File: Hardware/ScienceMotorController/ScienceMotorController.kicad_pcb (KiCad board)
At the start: 2 copper layers, 124.5 x 116.6 mm, 122 parts, among them U1 LM2576D2TR4, U2 TM4C129E_Launchpad, U3 VNH5019A_E, U4 VNH5019A_E, U5 VNH5019A_E, U6 VNH5019A_E, U7 VNH5019A_E, U8 VNH5019A_E

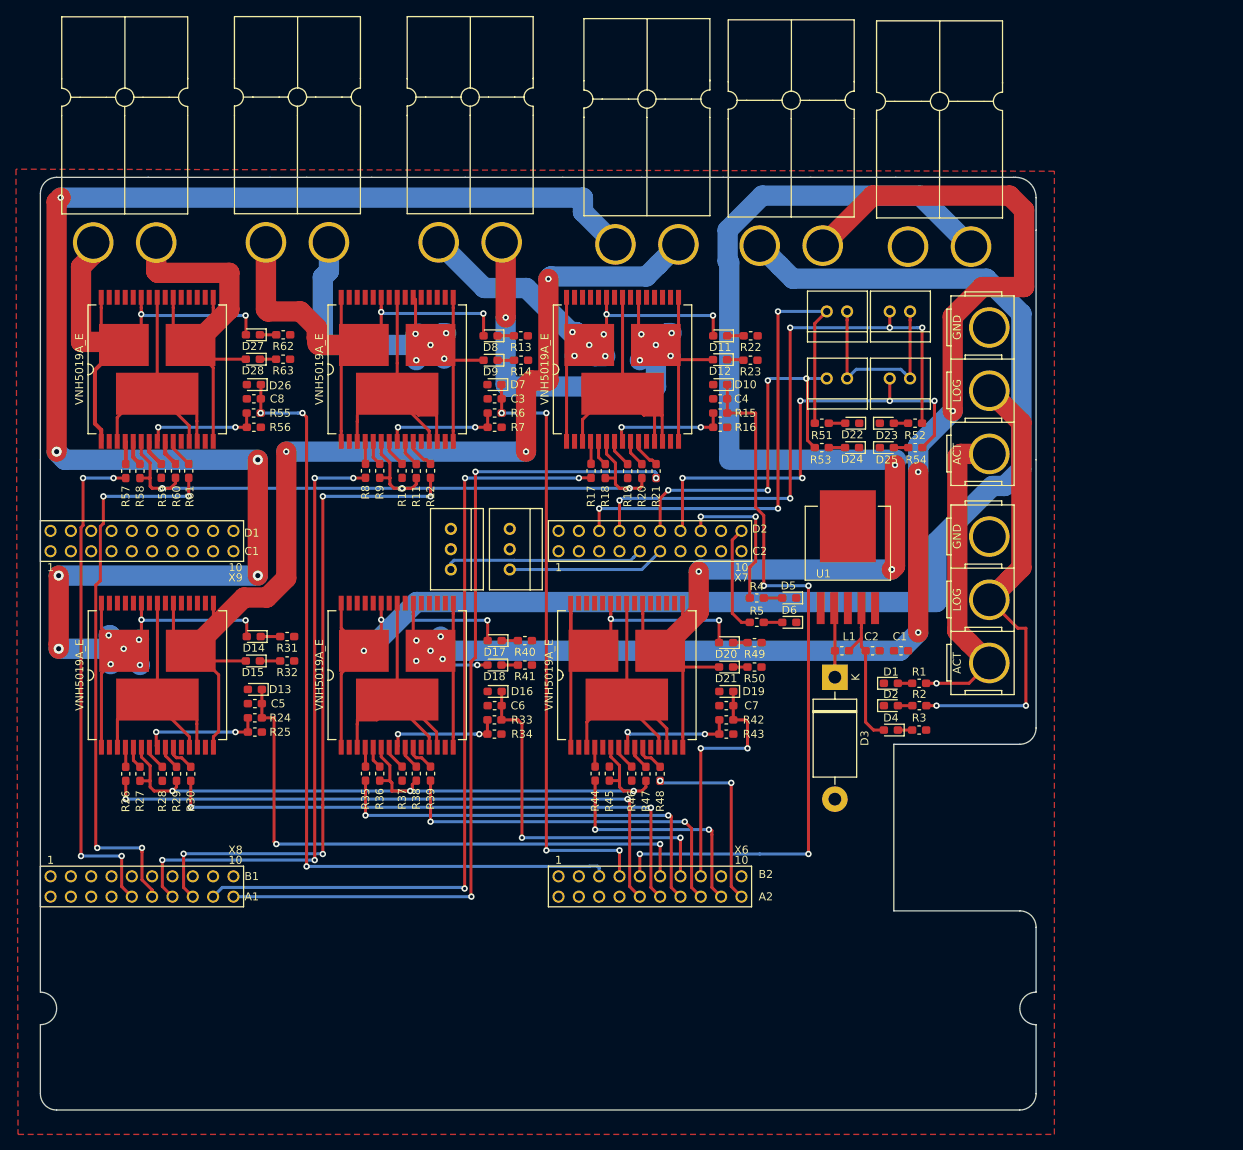
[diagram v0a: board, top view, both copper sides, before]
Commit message: routed more traces
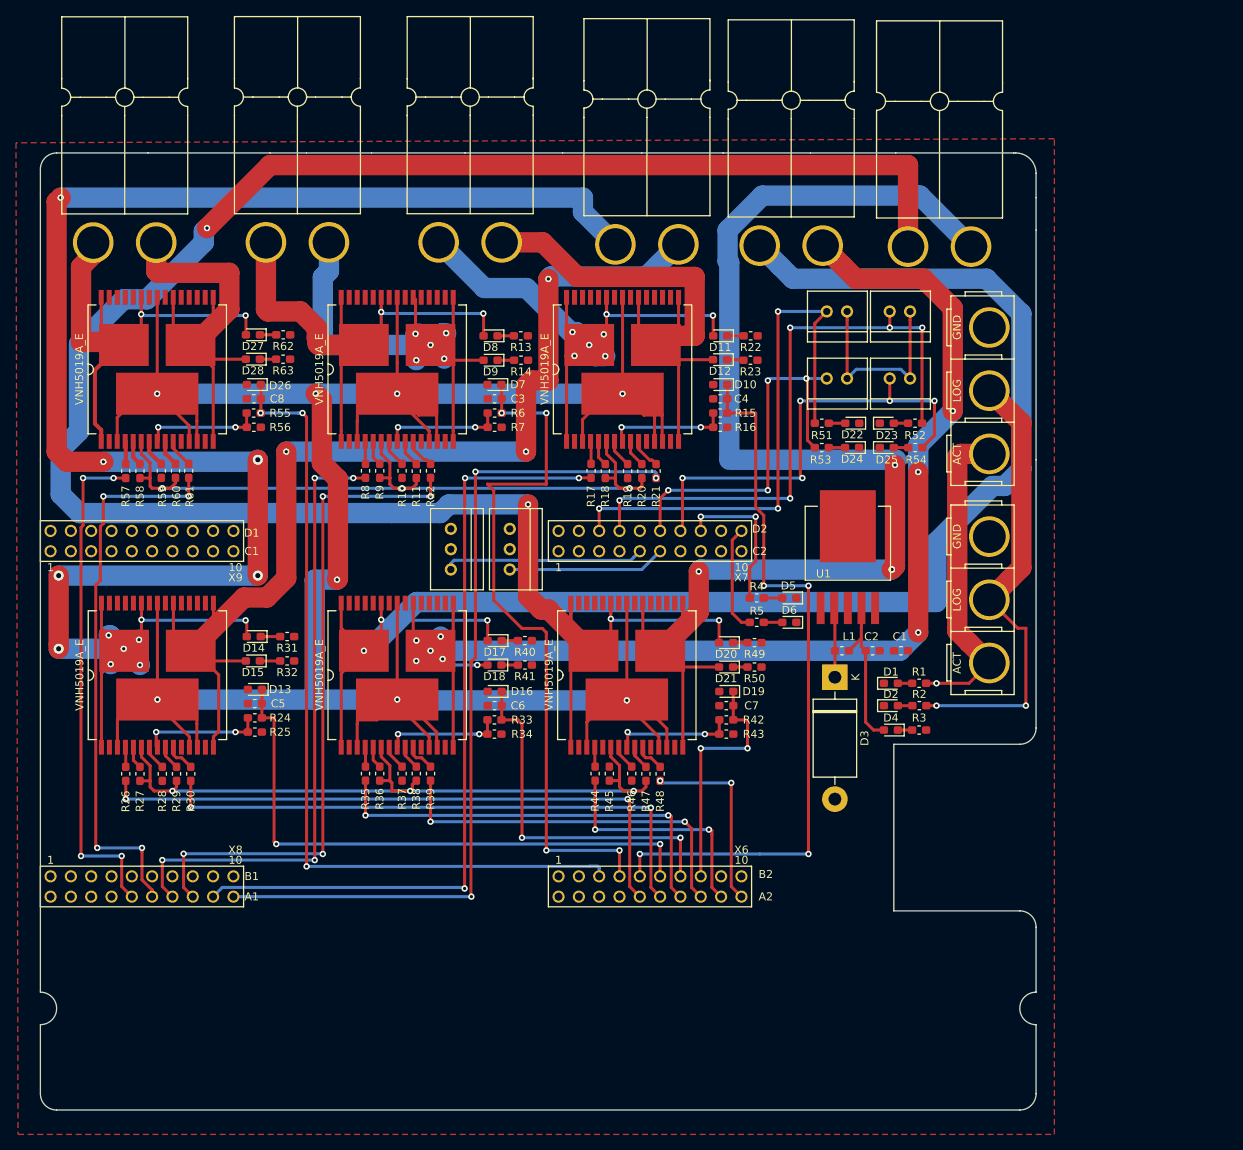
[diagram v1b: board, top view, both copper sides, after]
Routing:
- net Net-(Conn7-Pad2): track 49.0 -> 274.4 mm, vias 2 -> 4
- net +12VA: track 246.9 -> 406.0 mm, vias 1 -> 9
- net Net-(Conn6-Pad1): track 197.6 -> 169.9 mm
- net Net-(Conn4-Pad1): track 85.3 -> 70.3 mm, vias 6 -> 0
- net /Tiva/Motor Driver 2/Current_Sense_2: track 76.3 -> 88.2 mm
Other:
- board size 124.5 x 116.6 mm -> 124.5 x 119.6 mm

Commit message: finished routing traces
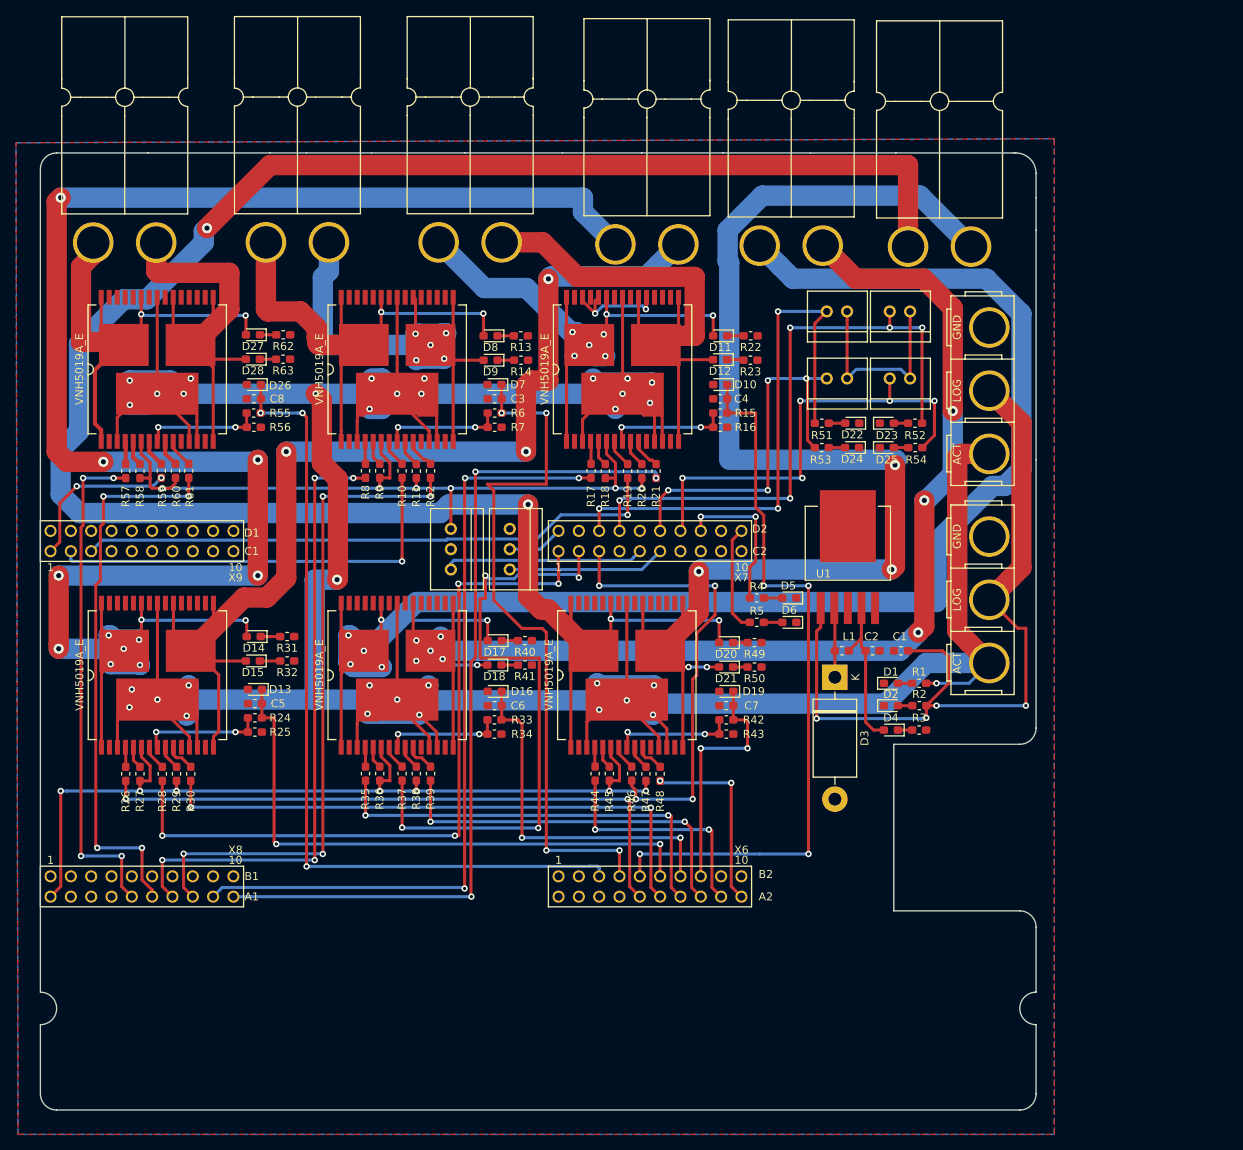
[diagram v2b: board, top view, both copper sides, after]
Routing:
- net +12VA: track 406.0 -> 551.6 mm, vias 9 -> 34
- net /Tiva/Motor Driver 4/PWM_4: track 0.00 -> 92.5 mm, vias 0 -> 4
- net /Tiva/Motor Driver 5/PWM_5: track 0.00 -> 78.0 mm, vias 0 -> 4
- net /Tiva/Motor Driver 3/PWM_3: track 0.00 -> 73.5 mm, vias 0 -> 1
- net /Tiva/Motor Driver 6/PWM_6: track 0.00 -> 56.3 mm, vias 0 -> 4
- net /Tiva/Motor Driver 2/PWM_2: track 0.00 -> 53.0 mm, vias 0 -> 1
- net /Power/12V: track 57.6 -> 99.6 mm, vias 2 -> 4
- net /Power/3.3V: track 229.8 -> 252.0 mm, vias 6 -> 13
- net /Tiva/Motor Driver 1/PWM_1: track 0.00 -> 20.5 mm, vias 0 -> 2
- net GND: track 0.00 -> 20.3 mm, vias 0 -> 2
- net Net-(Conn6-Pad2): track 194.7 -> 208.7 mm, vias 3 -> 6
- net Net-(Conn5-Pad2): track 241.0 -> 248.7 mm
- net Net-(Conn3-Pad1): track 68.5 -> 75.9 mm
- net Net-(R45-Pad1): track 0.00 -> 2.76 mm
- net Net-(Conn7-Pad1): vias 4 -> 5
- added copper zone on B.Cu, net /Power/3.3V

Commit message: fixed islands
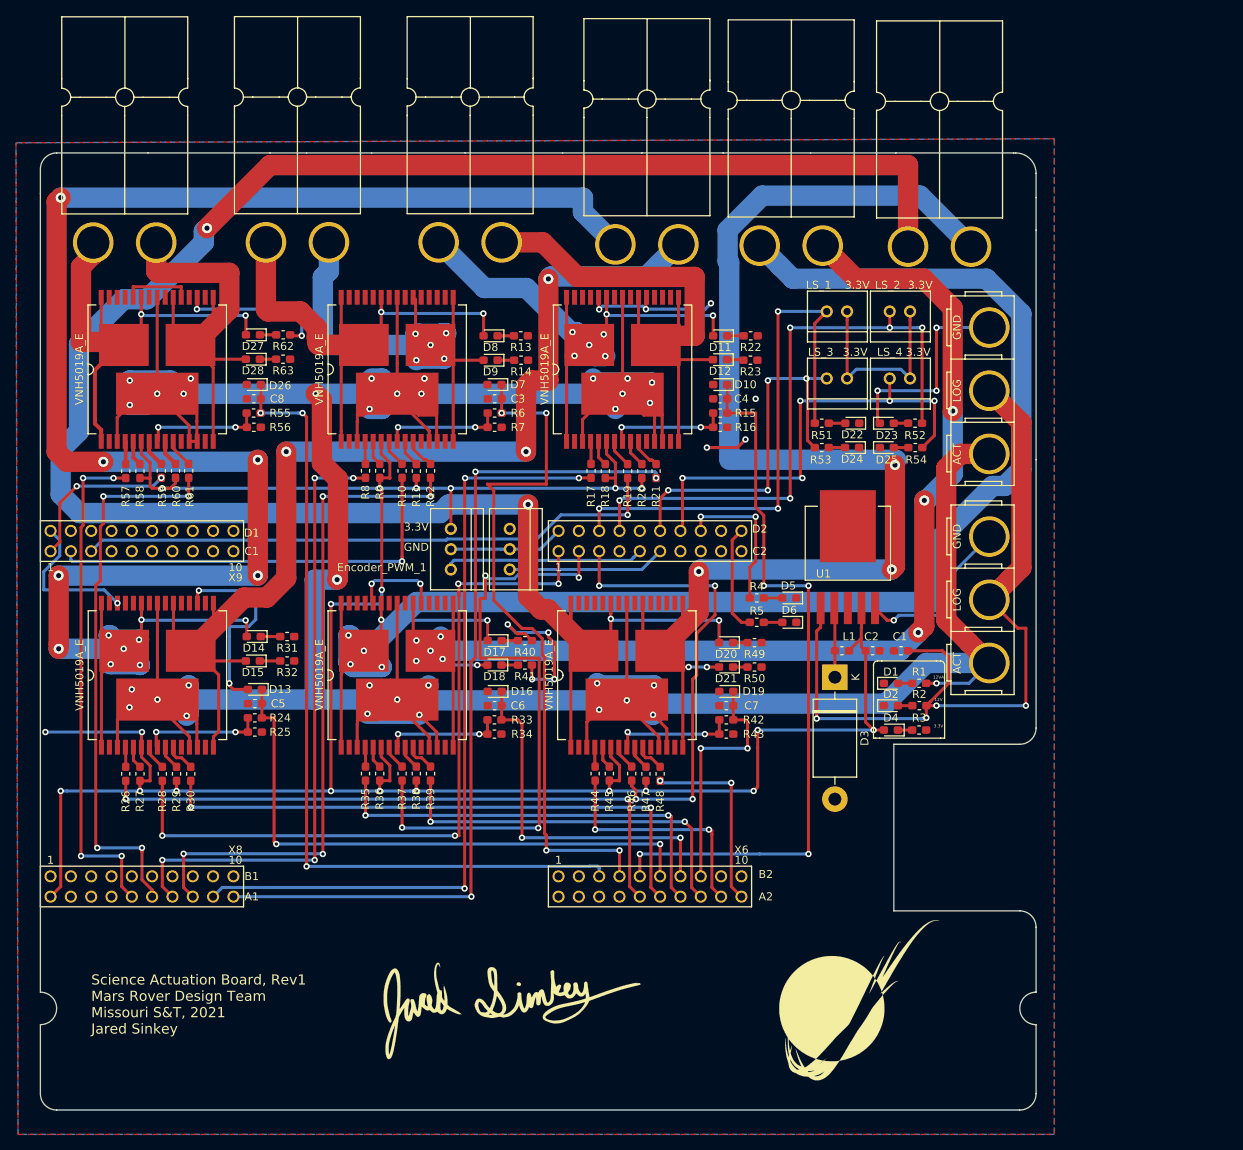
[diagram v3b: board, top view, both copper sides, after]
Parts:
- added G***: LOGO, MRDT_Silkscreens:0_MRDT_Logo_20mm, F.Cu at (136.9, 145.3)
- added G***: LOGO, MRDT_Silkscreens:0_MRDT_Logo_50mm, B.Cu at (110.2, 79.2)
- added G***: LOGO, MRDT_Silkscreens:z_sig_Jared_Sinkey_15.5mmx34.4mm, F.Cu at (93.7, 146.1)
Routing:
- net GND: track 20.3 -> 183.0 mm, vias 2 -> 18
- net /Power/3.3V: track 252.0 -> 351.3 mm, vias 13 -> 24
- net +12VA: track 551.6 -> 554.4 mm
- net Net-(Conn5-Pad1): track 139.0 -> 140.4 mm
- net /Tiva/Motor Driver 2/Current_Sense_2: track 88.2 -> 87.4 mm
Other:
- board text added: "12V"
- board text added: "12VA"
- board text added: "3.3V"
- board text added: "Encoder_PWM_1"
- board text added: "GND"
- board text added: "LS_1"
- board text added: "LS_2"
- board text added: "LS_3"
- board text added: "LS_4"
- board text added: "Science Actuation Board, Rev1 Mars Rover Design Team Missouri S&T, 2021 Jared Sinkey"

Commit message: added oki and began rerouting traces
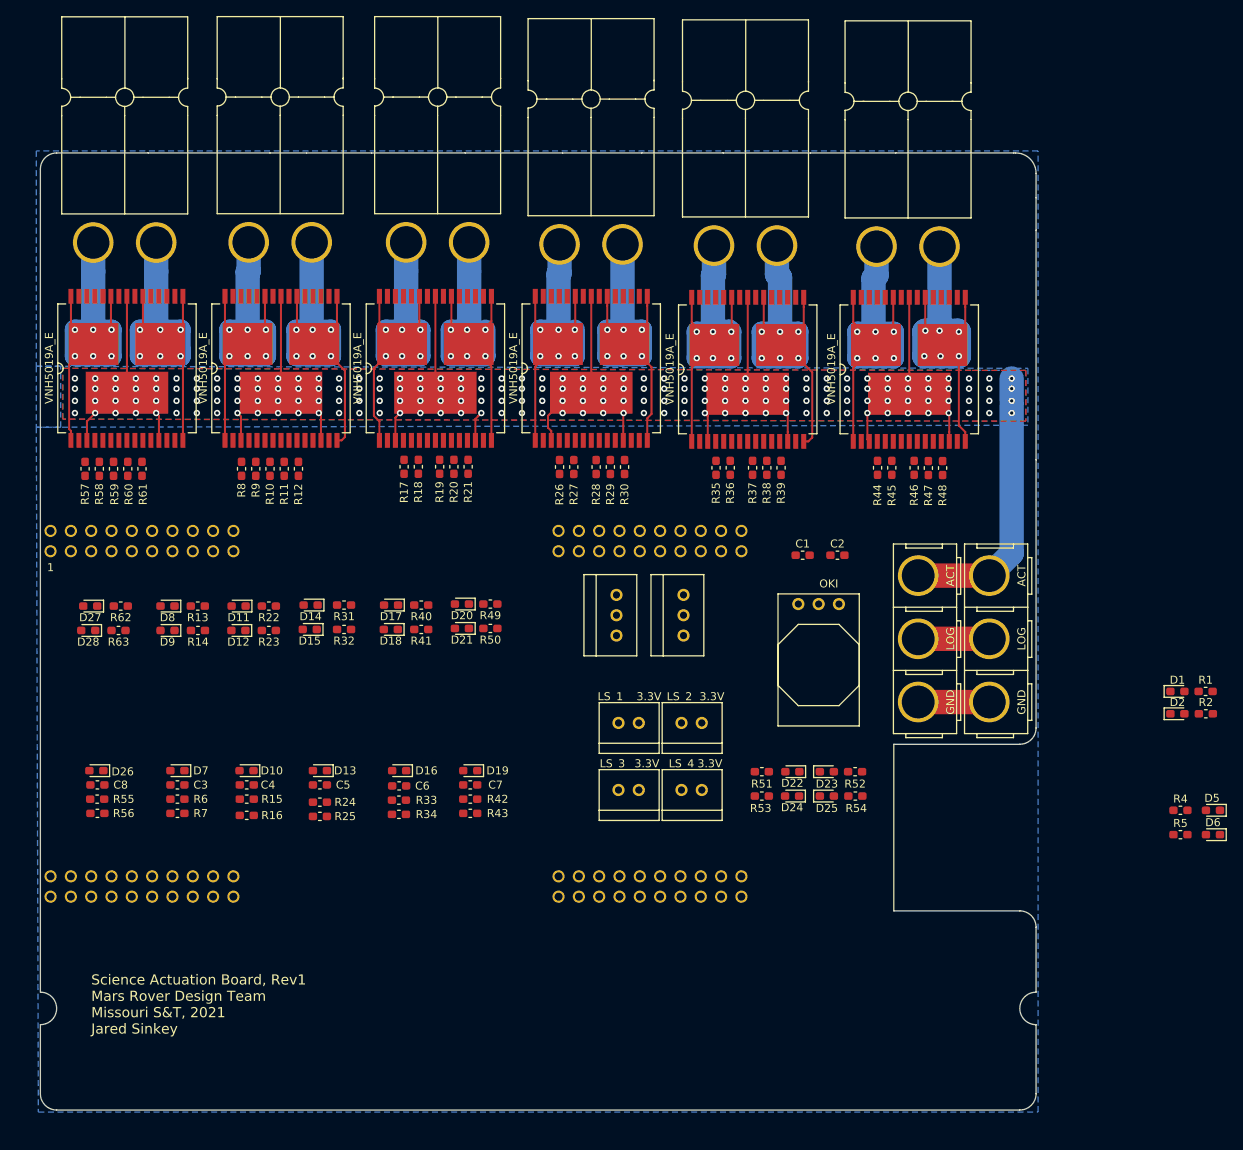
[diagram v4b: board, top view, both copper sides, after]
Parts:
- removed D3: D_Schottky_Small, Diode_THT:D_DO-201AD_P15.24mm_Horizontal
- removed D4: LED, LED_SMD:LED_0603_1608Metric_Pad1.05x0.95mm_HandSolder
- removed G***: LOGO, MRDT_Silkscreens:0_MRDT_Logo_20mm
- removed G***: LOGO, MRDT_Silkscreens:0_MRDT_Logo_50mm
- removed G***: LOGO, MRDT_Silkscreens:z_sig_Jared_Sinkey_15.5mmx34.4mm
- removed L1: 100uH, Inductor_SMD:L_0603_1608Metric_Pad1.05x0.95mm_HandSolder
- removed R3: 330, Resistor_SMD:R_0603_1608Metric_Pad1.05x0.95mm_HandSolder
- C1: value 100uF -> 10uF
- C2: value 1000uF -> 10uF
- U1: value LM2576D2TR4 -> OKI; footprint MRDT_Devices:LM2576 -> MRDT_Devices:OKI_Horizontal
- U2: footprint MRDT_Shields:TM4C129E_Launchpad_FULL_THT_TOP -> MRDT_Shields:TM4C129E_Launchpad_FULL_THT_BOTTOM
- moved R16 76.5 mm to (60.3, 122.2)
- moved D10 76.4 mm to (60.3, 116.6)
- moved C4 76.4 mm to (60.3, 118.4)
- moved R15 76.4 mm to (60.3, 120.1)
- moved D12 69.1 mm to (59.3, 99.1)
- moved R22 69.1 mm to (63.1, 96.0)
- moved D11 69.0 mm to (59.3, 96.0)
- moved R23 69.0 mm to (63.1, 99.1)
- moved R28 66.4 mm to (104.0, 78.6)
- moved U5 66.4 mm to (96.4, 75.3)
- moved R26 66.4 mm to (99.4, 78.6)
- moved R27 66.4 mm to (101.2, 78.6)
- moved R29 66.4 mm to (105.8, 78.6)
- moved R30 66.4 mm to (107.6, 78.6)
- moved C3 62.5 mm to (51.7, 118.4)
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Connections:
- C1 pad 1: GND -> /Power/12V
- C1 pad 2: /Power/12V -> GND
- U1 pad 2: Net-(D3-Pad1) -> GND
- U1 pad 3: GND -> /Power/3.3V
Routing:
- net +12VA: track 554.4 -> 167.8 mm, vias 34 -> 188
- net /Power/3.3V: track 351.3 -> 0.00 mm, vias 24 -> 0
- net Net-(Conn7-Pad2): track 274.4 -> 55.5 mm, vias 4 -> 6
- net Net-(Conn5-Pad2): track 248.7 -> 53.4 mm, vias 13 -> 6
- net GND: track 183.0 -> 8.89 mm, vias 18 -> 0
- net Net-(Conn6-Pad2): track 208.7 -> 55.4 mm
- net Net-(Conn7-Pad1): track 170.1 -> 54.6 mm, vias 5 -> 6
- net Net-(Conn6-Pad1): track 170.1 -> 56.7 mm, vias 9 -> 6
- net /Tiva/Motor Driver 3/In_B_3: track 106.4 -> 0.00 mm, vias 3 -> 0
- net /Tiva/Motor Driver 1/Current_Sense_1: track 103.4 -> 0.00 mm, vias 3 -> 0
- net /Tiva/Motor Driver 3/In_A_3: track 99.1 -> 0.00 mm, vias 3 -> 0
- net /Tiva/Motor Driver 4/PWM_4: track 92.5 -> 0.00 mm, vias 4 -> 0
- net /Tiva/Motor Driver 3/Current_Sense_3: track 92.1 -> 0.00 mm, vias 4 -> 0
- net /Power/12V: track 99.6 -> 8.89 mm, vias 4 -> 0
- net /Tiva/Motor Driver 2/Current_Sense_2: track 87.4 -> 0.00 mm, vias 4 -> 0
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- added copper zone on B.Cu, net (none)
- added copper zone on B.Cu, net +12VA
- added copper zone on F.Cu, net +12VA
- added copper zone on B.Cu, net GND
- removed copper zone on B.Cu, net /Power/3.3V
- removed copper zone on F.Cu, net GND
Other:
- board text removed: "12V"
- board text removed: "12VA"
- board text removed: "Encoder_PWM_1"
- board text removed: "GND"
